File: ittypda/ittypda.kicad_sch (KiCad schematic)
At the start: 147 parts, among them CN1 S2B-PH-SM4-TB, J1 USB_C_Receptacle_USB2.0_14P, SW1 Switch, SW10 Switch, SW11 Switch, SW12 Switch, SW13 Switch, SW14 Switch, SW15 Switch, SW16 Switch, SW17 Switch, SW18 Switch, SW19 Switch, SW2 Switch, SW20 Switch, SW21 Switch, SW22 Switch, SW23 Switch, SW24 Switch, SW26 Switch, SW27 Switch, SW28 Switch, SW29 Switch, SW3 Switch, SW30 Switch, SW31 Switch, SW32 Switch, SW33 Switch, SW34 Switch, SW36 Switch, SW37 Switch, SW38 Switch, SW39 Switch, SW4 Switch, SW41 Switch, SW42 Switch, SW43 Switch, SW44 Switch, SW45 Switch, SW46 Switch, SW47 Switch, SW48 Switch, SW49 Switch, SW5 Switch, SW50 Switch, SW51 Switch, SW52 Switch, SW53 Switch, SW54 Switch, SW55 Switch, SW56 Switch, SW57 Switch, SW58 Switch, SW59 Switch, SW6 Switch, SW60 Switch, SW61 Switch, SW62 SW_SPDT, SW7 Switch, SW8 Switch, SW9 Switch, U1 STM32F401RETx, U2 BQ24040DSQR, U3 TLV75801PDRV, Y1 16Mhz

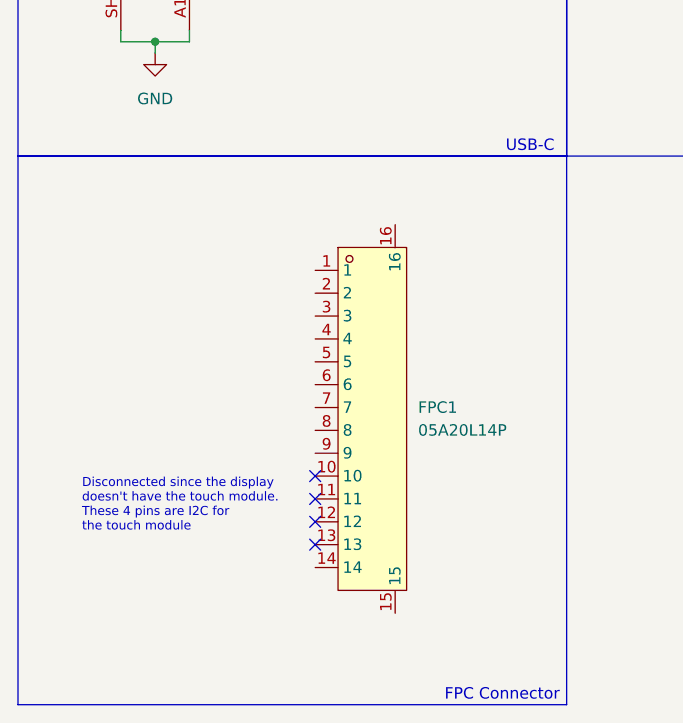
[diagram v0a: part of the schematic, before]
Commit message: add labels to FPC connector pins
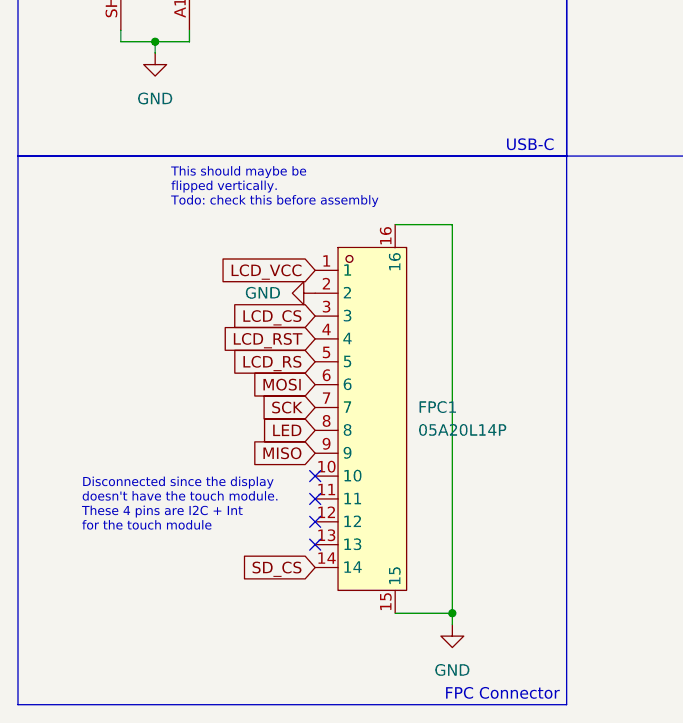
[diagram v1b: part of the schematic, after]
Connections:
- net GND: now also FPC1.15, FPC1.16, FPC1.2
- net LCD_VCC: now reaches FPC1.1
- net SD_CS: now reaches FPC1.14
- net LCD_CS: now reaches FPC1.3
- net LCD_RST: now reaches FPC1.4
- net LCD_RS: now reaches FPC1.5
- net MOSI: now reaches FPC1.6
- net SCK: now reaches FPC1.7
- net LED: now reaches FPC1.8
- net MISO: now reaches FPC1.9
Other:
- note added: "Disconnected since the display doesn't have the touch module. These 4 pins are I2C + Int for the touch module"
- note added: "This should maybe be flipped vertically. Todo: check this before assembly"
- note removed: "Disconnected since the display doesn't have the touch module. These 4 pins are I2C for the touch module"

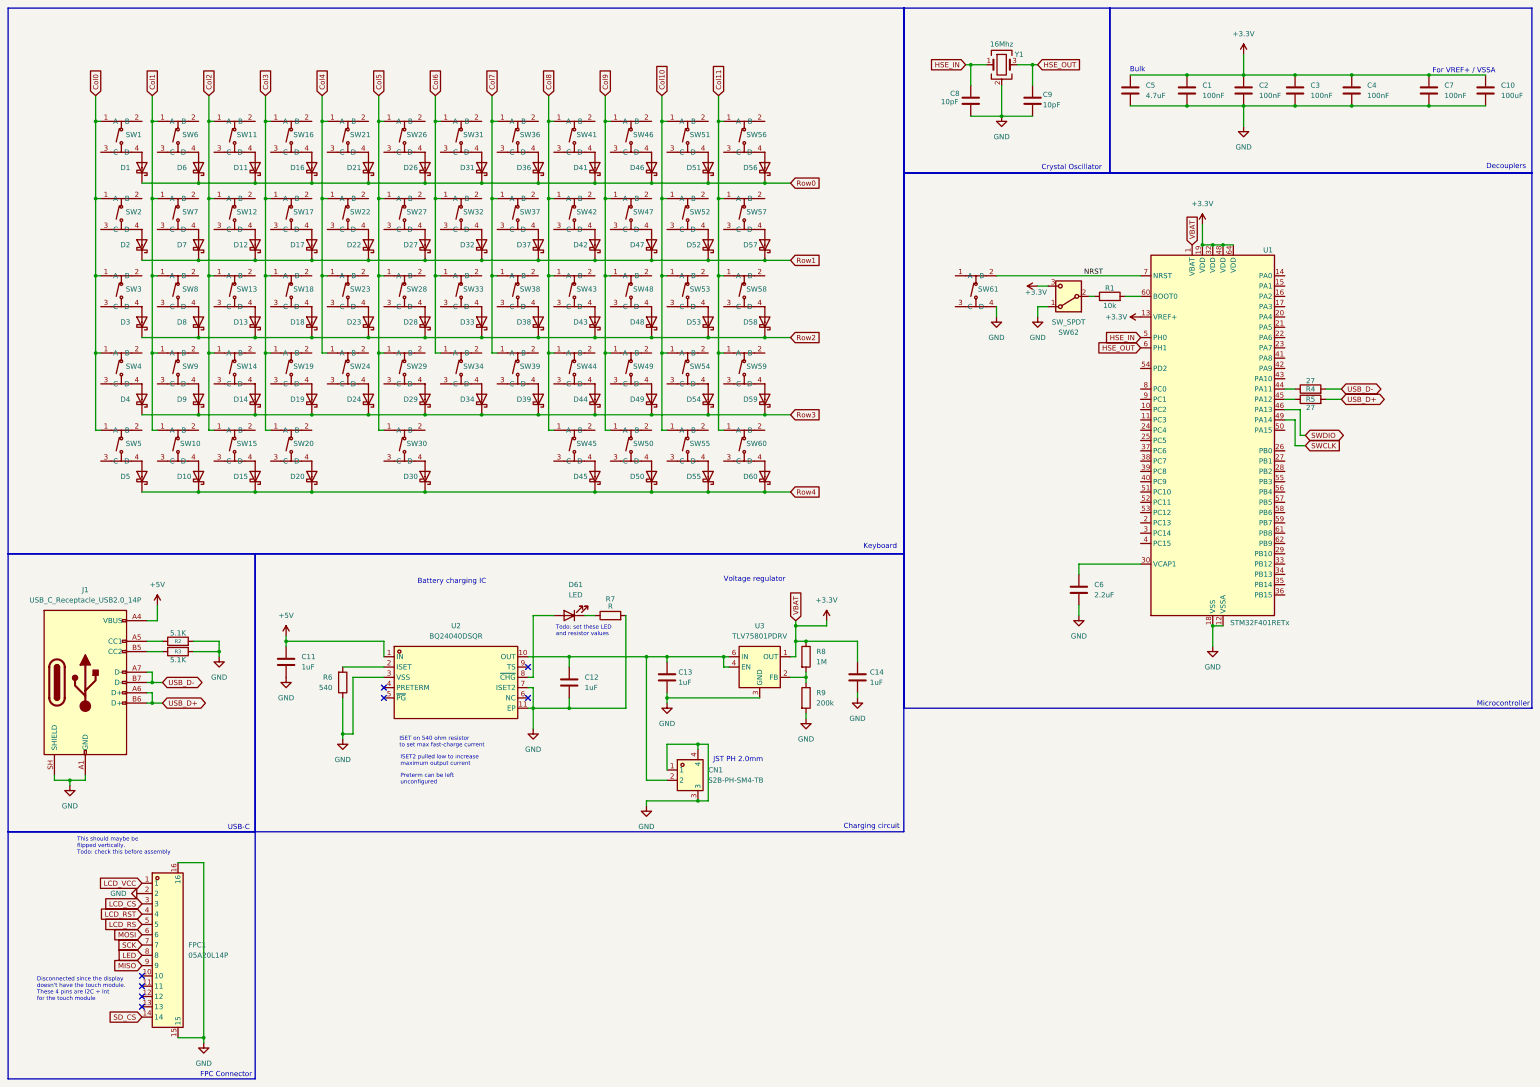
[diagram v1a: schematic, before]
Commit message: add debug pins
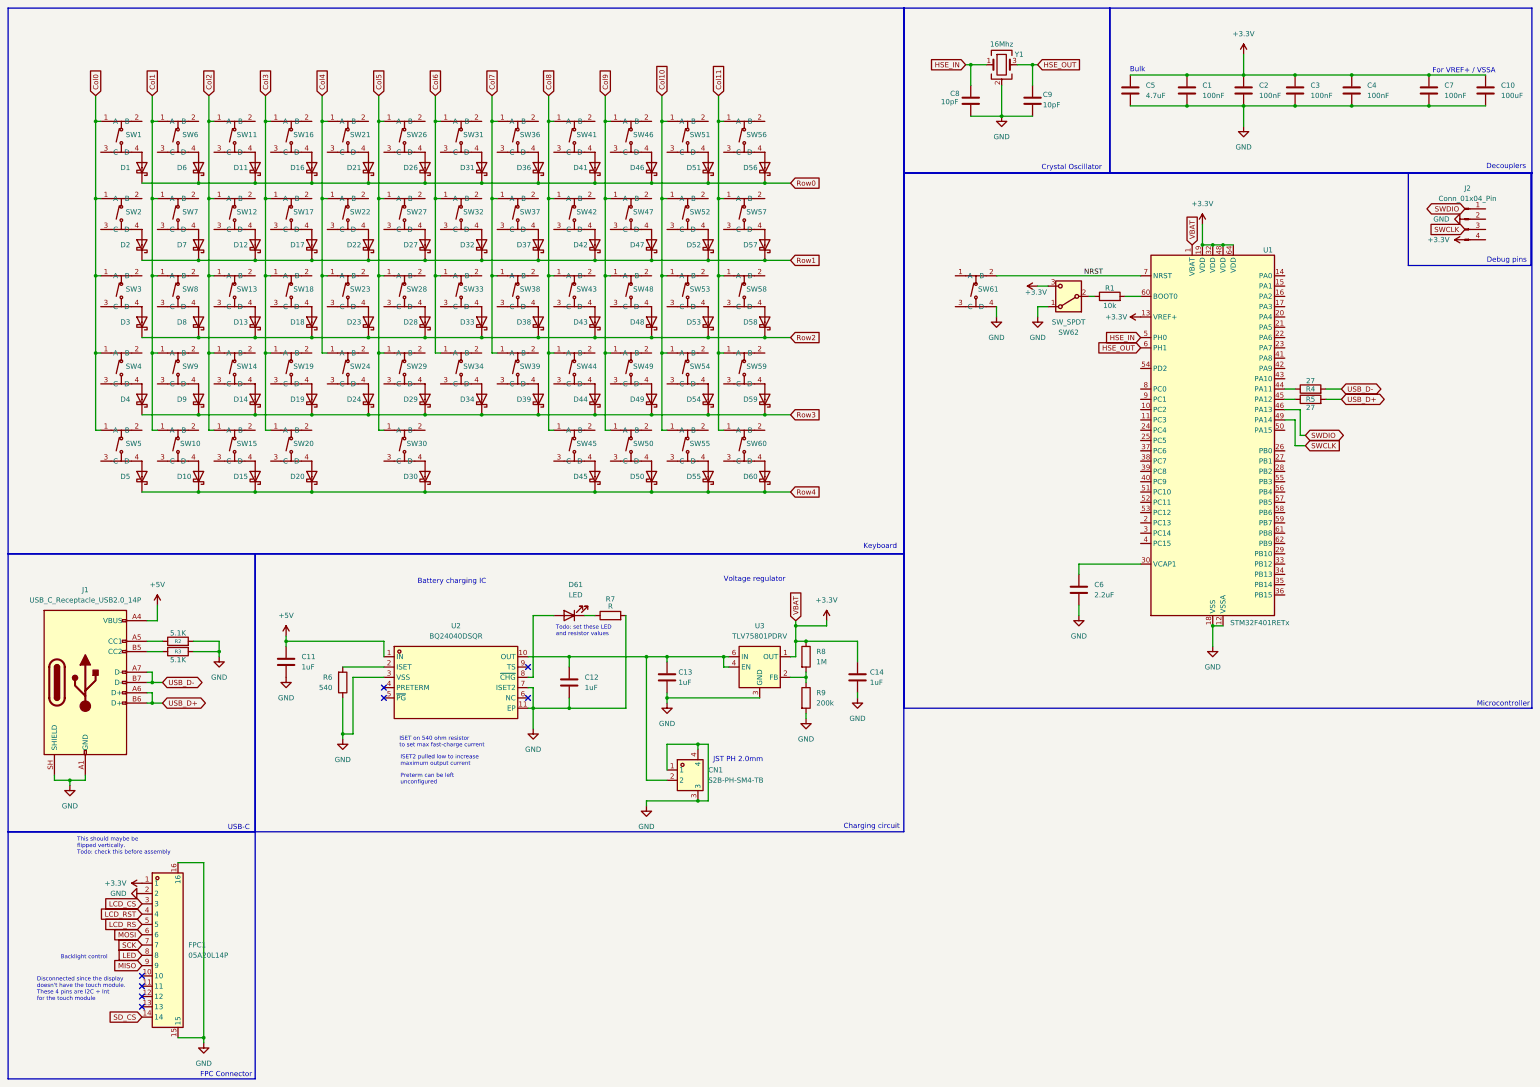
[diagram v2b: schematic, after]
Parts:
- added J2: Conn_01x04_Pin, symbol Connector:Conn_01x04_Pin
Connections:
- net LCD_VCC is gone; now on net +3.3V: FPC1.1
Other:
- note added: "Backlight control"
- note added: "Debug pins"

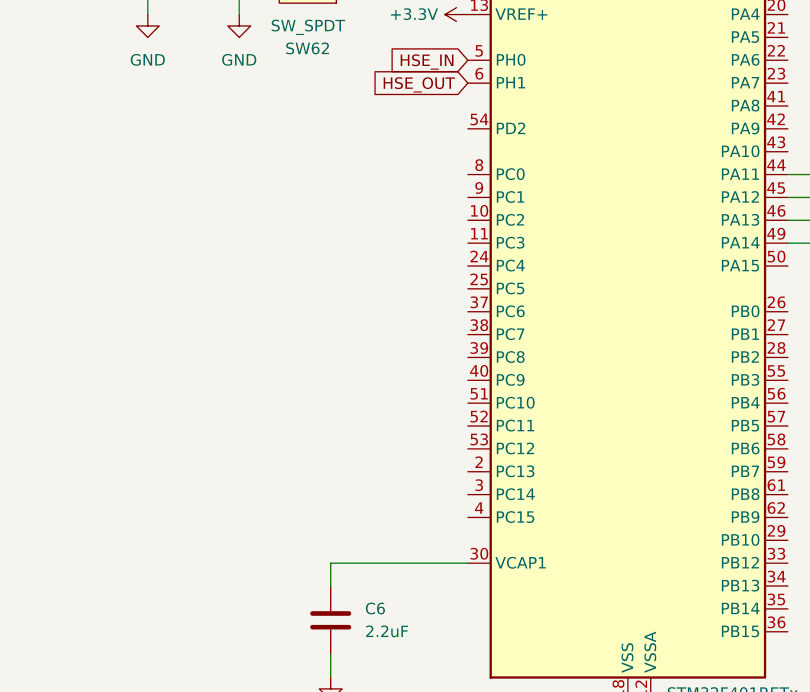
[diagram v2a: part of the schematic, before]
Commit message: connect FPC pins to ic gpios
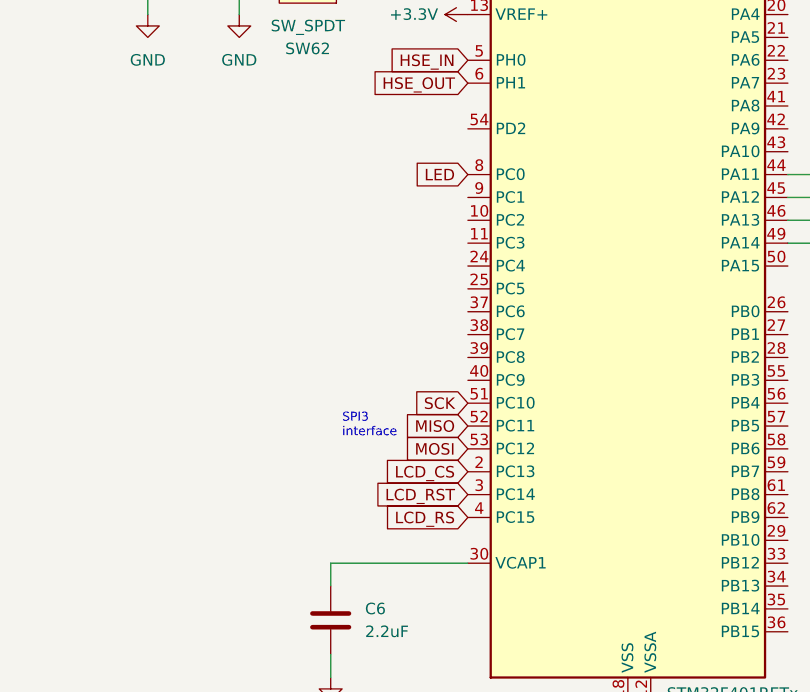
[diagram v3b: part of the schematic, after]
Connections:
- net LCD_CS: now also U1.2 (PC13)
- net LCD_RS: now also U1.4 (PC15)
- net LCD_RST: now also U1.3 (PC14)
- net LED: now also U1.8 (PC0)
- net MISO: now also U1.52 (PC11)
- net MOSI: now also U1.53 (PC12)
- net SCK: now also U1.51 (PC10)
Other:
- note added: "SPI3 interface"
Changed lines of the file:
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@@
 		)
 	)
+	(text "SPI3\ninterface"
+		(exclude_from_sim no)
+		(at 280.67 139.7 0)
+		(effects
+			(font
+				(size 1 1)
+			)
+			(justify left)
+		)
+	)
 	(text "Keyboard\n"
 		(exclude_from_sim no)
@@
 		)
 	)
+	(global_label "LCD_CS"
+		(shape input)
+		(at 294.64 144.78 180)
+		(fields_autoplaced yes)
+		(effects
+			(font
+				(size 1.27 1.27)
+			)
+			(justify right)
+		)
+		(property "Intersheetrefs" "${INTERSHEET_REFS}"
+			(at 284.6396 144.78 0)
+			(hide yes)
+			(show_name no)
+			(do_not_autoplace no)
+			(effects
+				(font
+					(size 1.27 1.27)
+				)
+				(justify right)
+			)
+		)
+	)
 	(global_label "Col10"
 		(shape input)
@@
 		)
 	)
+	(global_label "MOSI"
+		(shape input)
+		(at 294.64 142.24 180)
+		(fields_autoplaced yes)
+		(effects
+			(font
+				(size 1.27 1.27)
+			)
+			(justify right)
+		)
+		(property "Intersheetrefs" "${INTERSHEET_REFS}"
+			(at 287.0586 142.24 0)
+			(hide yes)
+			(show_name no)
+			(do_not_autoplace no)
+			(effects
+				(font
+					(size 1.27 1.27)
+				)
+				(justify right)
+			)
+		)
+	)
 	(global_label "VBAT"
 		(shape input)
@@
 		)
 	)
+	(global_label "LCD_RS"
+		(shape input)
+		(at 294.64 149.86 180)
+		(fields_autoplaced yes)
+		(effects
+			(font
+				(size 1.27 1.27)
+			)
+			(justify right)
+		)
+		(property "Intersheetrefs" "${INTERSHEET_REFS}"
+			(at 284.6396 149.86 0)
+			(hide yes)
+			(show_name no)
+			(do_not_autoplace no)
+			(effects
+				(font
+					(size 1.27 1.27)
+				)
+				(justify right)
+			)
+		)
+	)
+	(global_label "SCK"
+		(shape input)
+		(at 294.64 137.16 180)
+		(fields_autoplaced yes)
+		(effects
+			(font
+				(size 1.27 1.27)
+			)
+			(justify right)
+		)
+		(property "Intersheetrefs" "${INTERSHEET_REFS}"
+			(at 287.9053 137.16 0)
+			(hide yes)
+			(show_name no)
+			(do_not_autoplace no)
+			(effects
+				(font
+					(size 1.27 1.27)
+				)
+				(justify right)
+			)
+		)
+	)
 	(global_label "Col11"
 		(shape input)
@@
 		)
 	)
+	(global_label "LED"
+		(shape input)
+		(at 294.64 111.76 180)
+		(fields_autoplaced yes)
+		(effects
+			(font
+				(size 1.27 1.27)
+			)
+			(justify right)
+		)
+		(property "Intersheetrefs" "${INTERSHEET_REFS}"
+			(at 288.2077 111.76 0)
+			(hide yes)
+			(show_name no)
+			(do_not_autoplace no)
+			(effects
+				(font
+					(size 1.27 1.27)
+				)
+				(justify right)
+			)
+		)
+	)
 	(global_label "Row2"
 		(shape input)
@@
 		)
 	)
+	(global_label "LCD_RST"
+		(shape input)
+		(at 294.64 147.32 180)
+		(fields_autoplaced yes)
+		(effects
+			(font
+				(size 1.27 1.27)
+			)
+			(justify right)
+		)
+		(property "Intersheetrefs" "${INTERSHEET_REFS}"
+			(at 283.672 147.32 0)
+			(hide yes)
+			(show_name no)
+			(do_not_autoplace no)
+			(effects
+				(font
+					(size 1.27 1.27)
+				)
+				(justify right)
+			)
+		)
+	)
 	(global_label "Col2"
 		(shape input)
@@
 			(hide yes)
 			(show_name no)
+			(do_not_autoplace no)
+			(effects
+				(font
+					(size 1.27 1.27)
+				)
+				(justify right)
+			)
+		)
+	)
+	(global_label "MISO"
+		(shape input)
+		(at 294.64 139.7 180)
+		(fields_autoplaced yes)
+		(effects
+			(font
+				(size 1.27 1.27)
+			)
+			(justify right)
+		)
+		(property "Intersheetrefs" "${INTERSHEET_REFS}"
+			(at 287.0586 139.7 0)
+			(hide yes)
+			(show_name no)

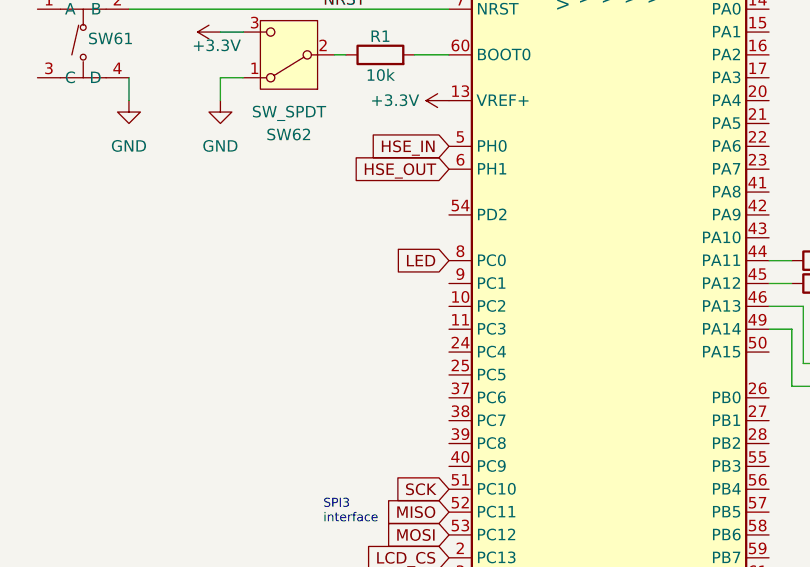
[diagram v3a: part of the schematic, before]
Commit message: add debug pins footprint
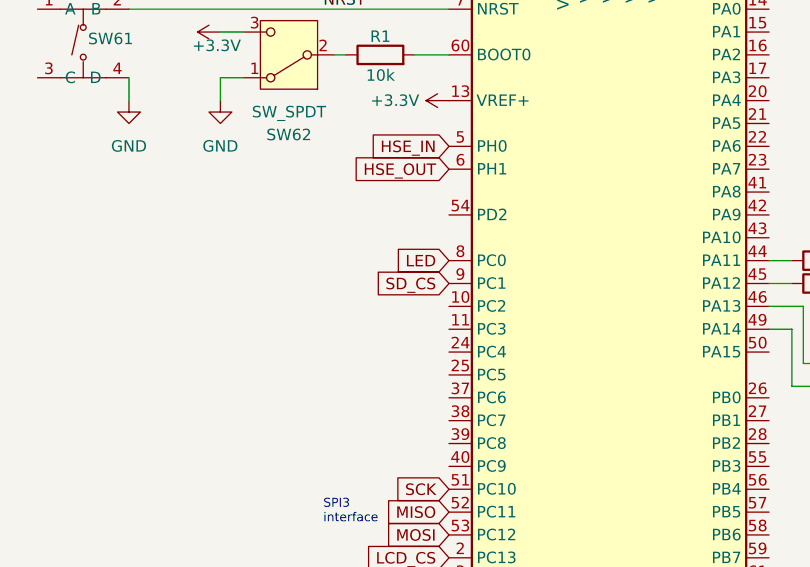
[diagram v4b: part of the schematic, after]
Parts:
- J2: footprint (none) -> Connector_PinHeader_2.54mm:PinHeader_1x04_P2.54mm_Vertical
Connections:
- net SD_CS: now also U1.9 (PC1)
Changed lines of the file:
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@@
 		)
 	)
+	(global_label "SD_CS"
+		(shape input)
+		(at 294.64 114.3 180)
+		(fields_autoplaced yes)
+		(effects
+			(font
+				(size 1.27 1.27)
+			)
+			(justify right)
+		)
+		(property "Intersheetrefs" "${INTERSHEET_REFS}"
+			(at 285.7282 114.3 0)
+			(hide yes)
+			(show_name no)
+			(do_not_autoplace no)
+			(effects
+				(font
+					(size 1.27 1.27)
+				)
+				(justify right)
+			)
+		)
+	)
 	(global_label "VBAT"
 		(shape input)
@@
 			)
 		)
-		(property "Footprint" ""
+		(property "Footprint" "Connector_PinHeader_2.54mm:PinHeader_1x04_P2.54mm_Vertical"
 			(at 374.65 69.85 0)
 			(hide yes)

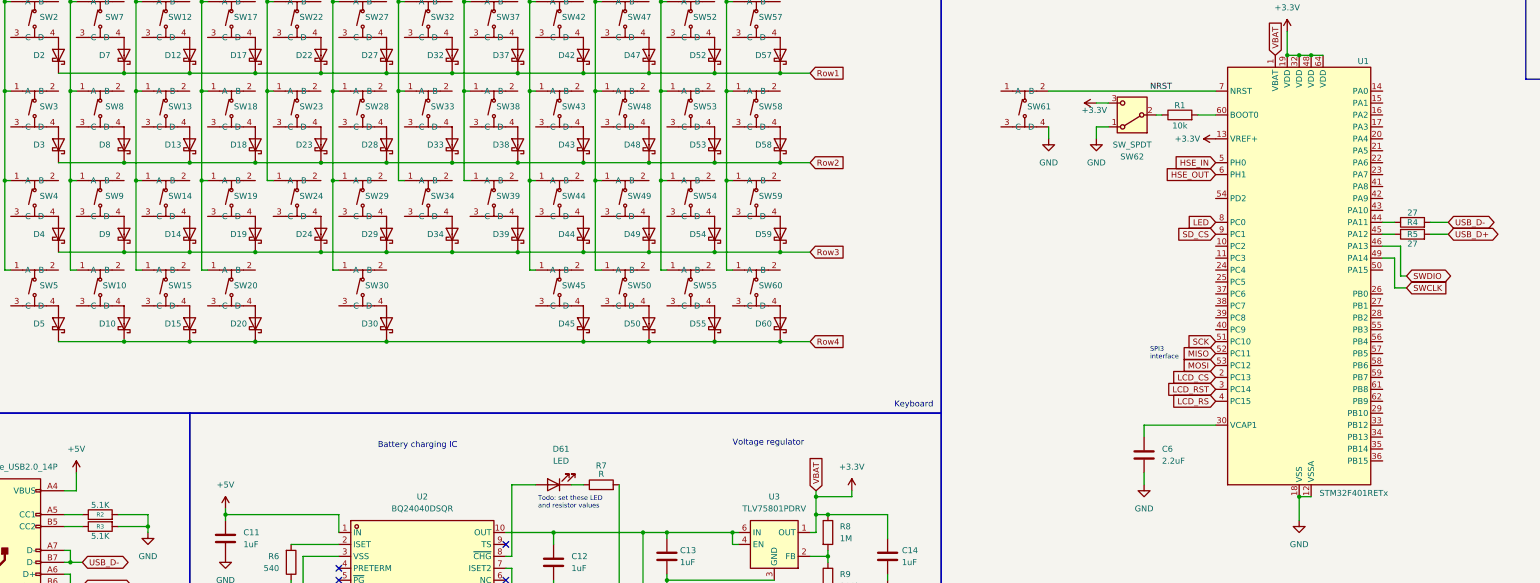
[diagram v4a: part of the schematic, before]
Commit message: connect keyboard matrix pins to GPIO
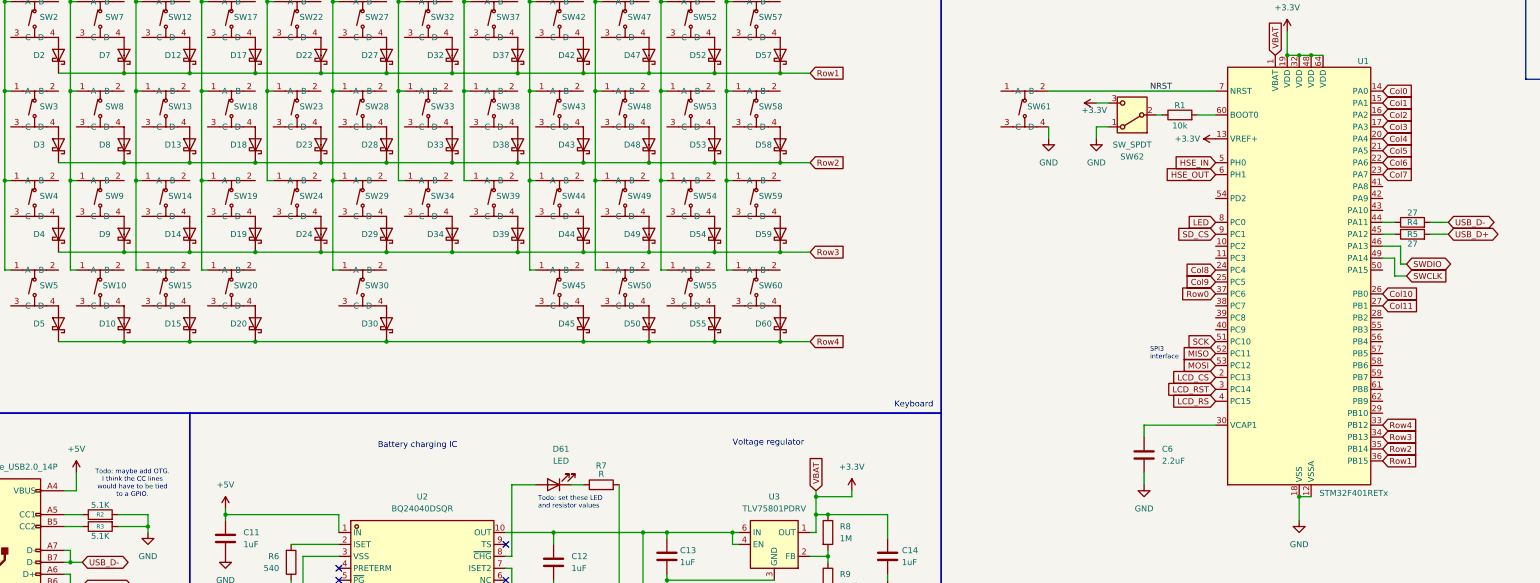
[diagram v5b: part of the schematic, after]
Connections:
- net Col0: now also U1.14 (PA0)
- net Col1: now also U1.15 (PA1)
- net Col10: now also U1.26 (PB0)
- net Col11: now also U1.27 (PB1)
- net Col2: now also U1.16 (PA2)
- net Col3: now also U1.17 (PA3)
- net Col4: now also U1.20 (PA4)
- net Col5: now also U1.21 (PA5)
- net Col6: now also U1.22 (PA6)
- net Col7: now also U1.23 (PA7)
- net Col8: now also U1.24 (PC4)
- net Col9: now also U1.25 (PC5)
- net Row0: now also U1.37 (PC6)
- net Row1: now also U1.36 (PB15)
- net Row2: now also U1.35 (PB14)
- net Row3: now also U1.34 (PB13)
- net Row4: now also U1.33 (PB12)
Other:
- note added: "Todo: maybe add OTG. I think the CC lines would have to be tied to a GPIO."
